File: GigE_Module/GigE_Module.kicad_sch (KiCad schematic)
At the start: 4 parts, among them J1 Conn_01x10_Socket, J3 Conn_01x02_Pin, J4 Conn_01x08_Socket, U4 ENC28J60x-SS

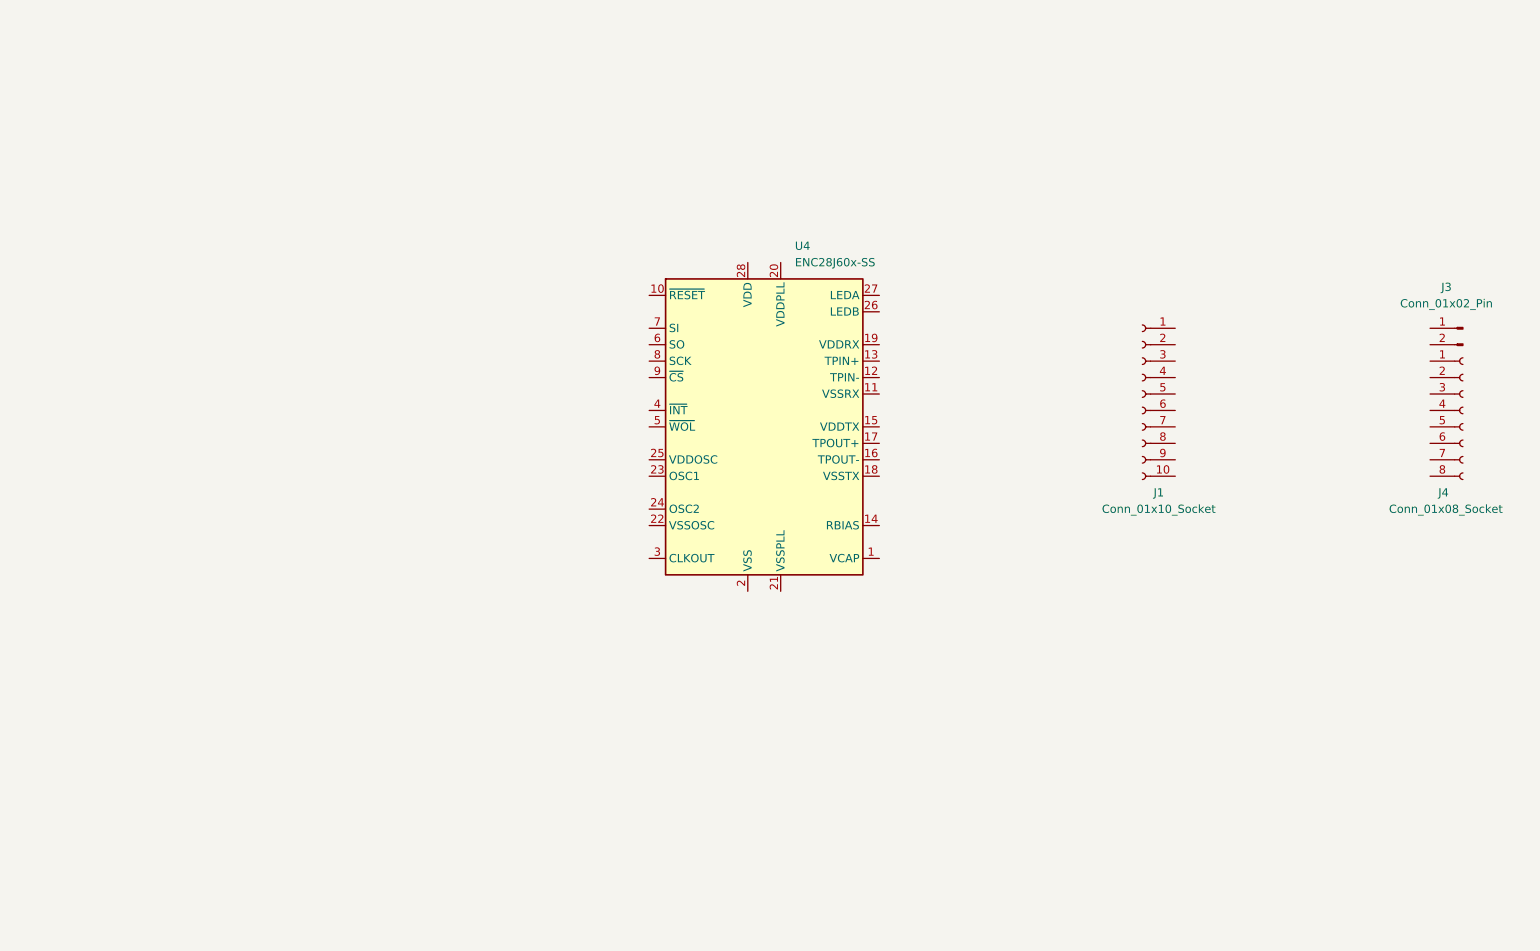
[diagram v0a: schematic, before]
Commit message: Adding GigE PCB design
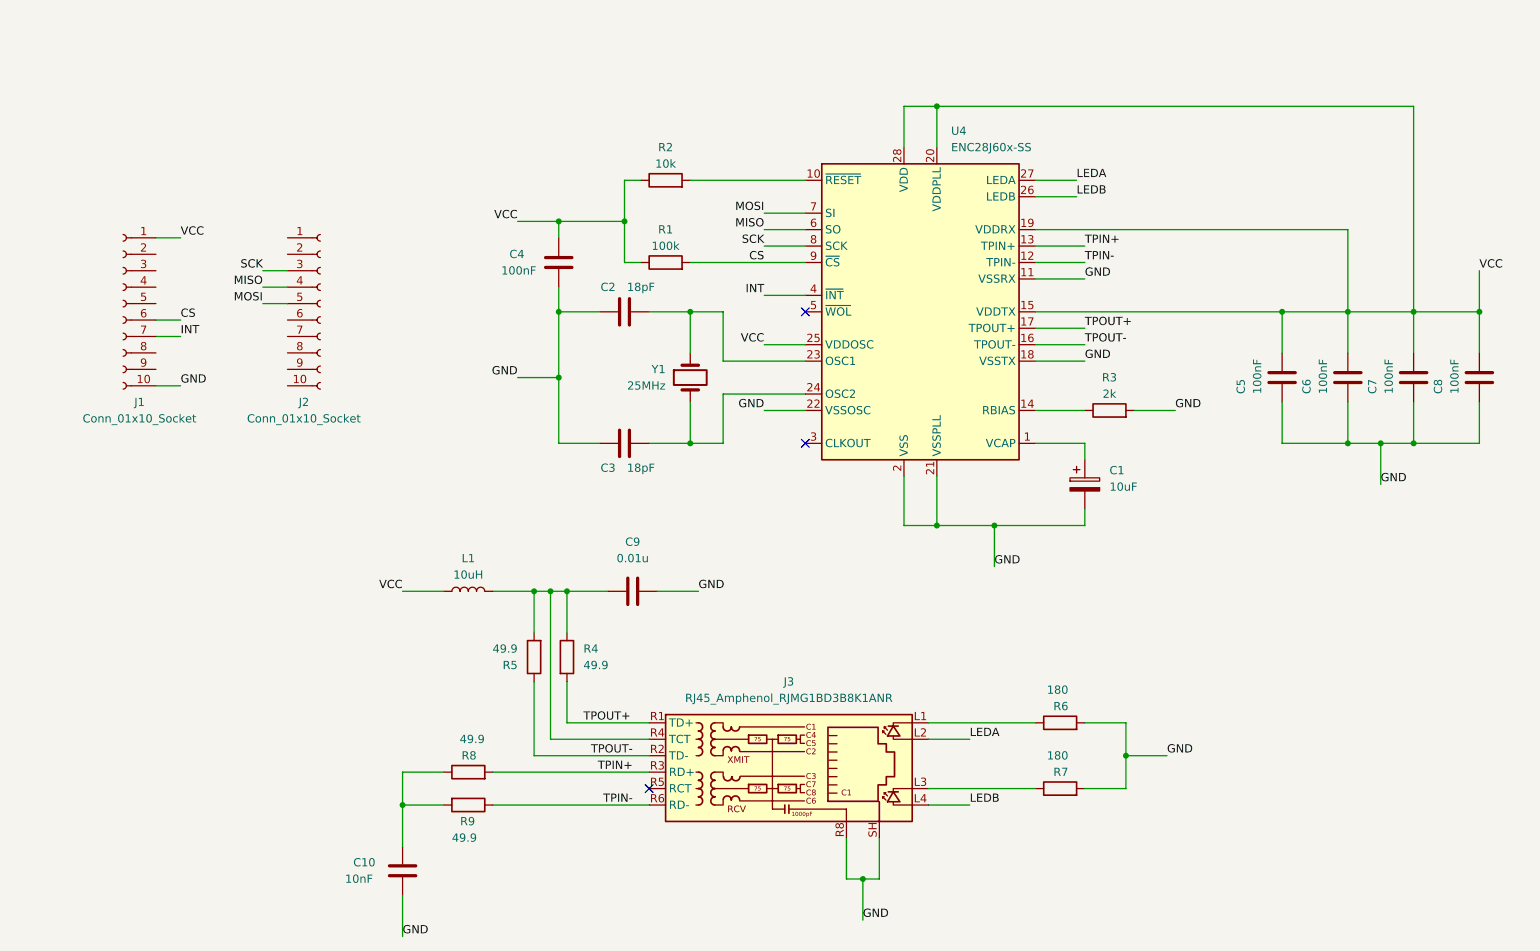
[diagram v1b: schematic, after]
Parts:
- removed J3: Conn_01x02_Pin, Connector_PinHeader_2.00mm:PinHeader_1x02_P2.00mm_Vertical, symbol Connector:Conn_01x02_Pin
- removed J4: Conn_01x08_Socket, Connector_PinSocket_2.00mm:PinSocket_1x08_P2.00mm_Vertical, symbol Connector:Conn_01x08_Socket
- added C1: 10uF, symbol Device:C_Polarized
- added C10: 10nF, symbol Device:C
- added C2, C3: 18pF, symbol Device:C
- added C4, C5, C6, C7, C8: 100nF, symbol Device:C
- added C9: 0.01u, symbol Device:C
- added J2: Conn_01x10_Socket, Connector_PinSocket_2.00mm:PinSocket_1x10_P2.00mm_Vertical, symbol Connector:Conn_01x10_Socket
- added J3: RJ45_Amphenol_RJMG1BD3B8K1ANR, Connector_RJ:RJ45_Amphenol_RJMG1BD3B8K1ANR, symbol Connector:RJ45_Amphenol_RJMG1BD3B8K1ANR
- added L1: 10uH, symbol Device:L
- added R1: 100k, symbol Device:R
- added R2: 10k, symbol Device:R
- added R3: 2k, symbol Device:R
- added R4, R5, R8, R9: 49.9, symbol Device:R
- added R6, R7: 180, symbol Device:R
- added Y1: 25MHz, symbol Device:Crystal
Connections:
- net VCC: now reaches J1.1 (Pin_1)
- net VCC: now also U4.15 (VDDTX), U4.19 (VDDRX), U4.20 (VDDPLL), U4.25 (VDDOSC), U4.28 (VDD), C4.1, C5.1, C6.1, C7.1, C8.1, L1.1, R1.1, R2.1
- net GND: now reaches J1.10 (Pin_10)
- net GND: now also U4.11 (VSSRX), U4.18 (VSSTX), U4.2 (VSS), U4.21 (VSSPLL), U4.22 (VSSOSC), C1.2, C10.2, C2.1, C3.1, C4.2, C5.2, C6.2, C7.2, C8.2, C9.2, J3.R8, J3.SH, R3.2, R6.2, R7.2
- net CS: now reaches J1.6 (Pin_6)
- net CS: now also U4.9 (~{CS}), R1.2
- net INT: now reaches J1.7 (Pin_7)
- net INT: now also U4.4 (~{INT})
- net at U4.1 (VCAP): now also C1.1
- net at U4.10 (~{RESET}): now also R2.2
- net TPIN-: now reaches U4.12 (TPIN-)
- net TPIN-: now also J3.R6 (RD-), R9.1
- net TPIN+: now reaches U4.13 (TPIN+)
- net TPIN+: now also J3.R3 (RD+), R8.2
- net at U4.14 (RBIAS): now also R3.1
- net TPOUT-: now reaches U4.16 (TPOUT-)
- net TPOUT-: now also J3.R2 (TD-), R5.1
- net TPOUT+: now reaches U4.17 (TPOUT+)
- net TPOUT+: now also J3.R1 (TD+), R4.2
- net at U4.23 (OSC1): now also C2.2, Y1.1
- net at U4.24 (OSC2): now also C3.2, Y1.2
- net LEDB: now reaches U4.26 (LEDB)
- net LEDB: now also J3.L4
- net LEDA: now reaches U4.27 (LEDA)
- net LEDA: now also J3.L2
- net MISO: now reaches U4.6 (SO)
- net MISO: now also J2.4 (Pin_4)
- net MOSI: now reaches U4.7 (SI)
- net MOSI: now also J2.5 (Pin_5)
- net SCK: now reaches U4.8 (SCK)
- net SCK: now also J2.3 (Pin_3)
- new net: C9.1, J3.R4 (TCT), L1.2, R4.1, R5.2
- new net: C10.1, R8.1, R9.2
- new net: J3.L1, R6.1
- new net: J3.L3, R7.1
- no-connect marks 0 -> 3
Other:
- moved on the sheet: J1, U4

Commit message: Adding first version of GigE PCB design
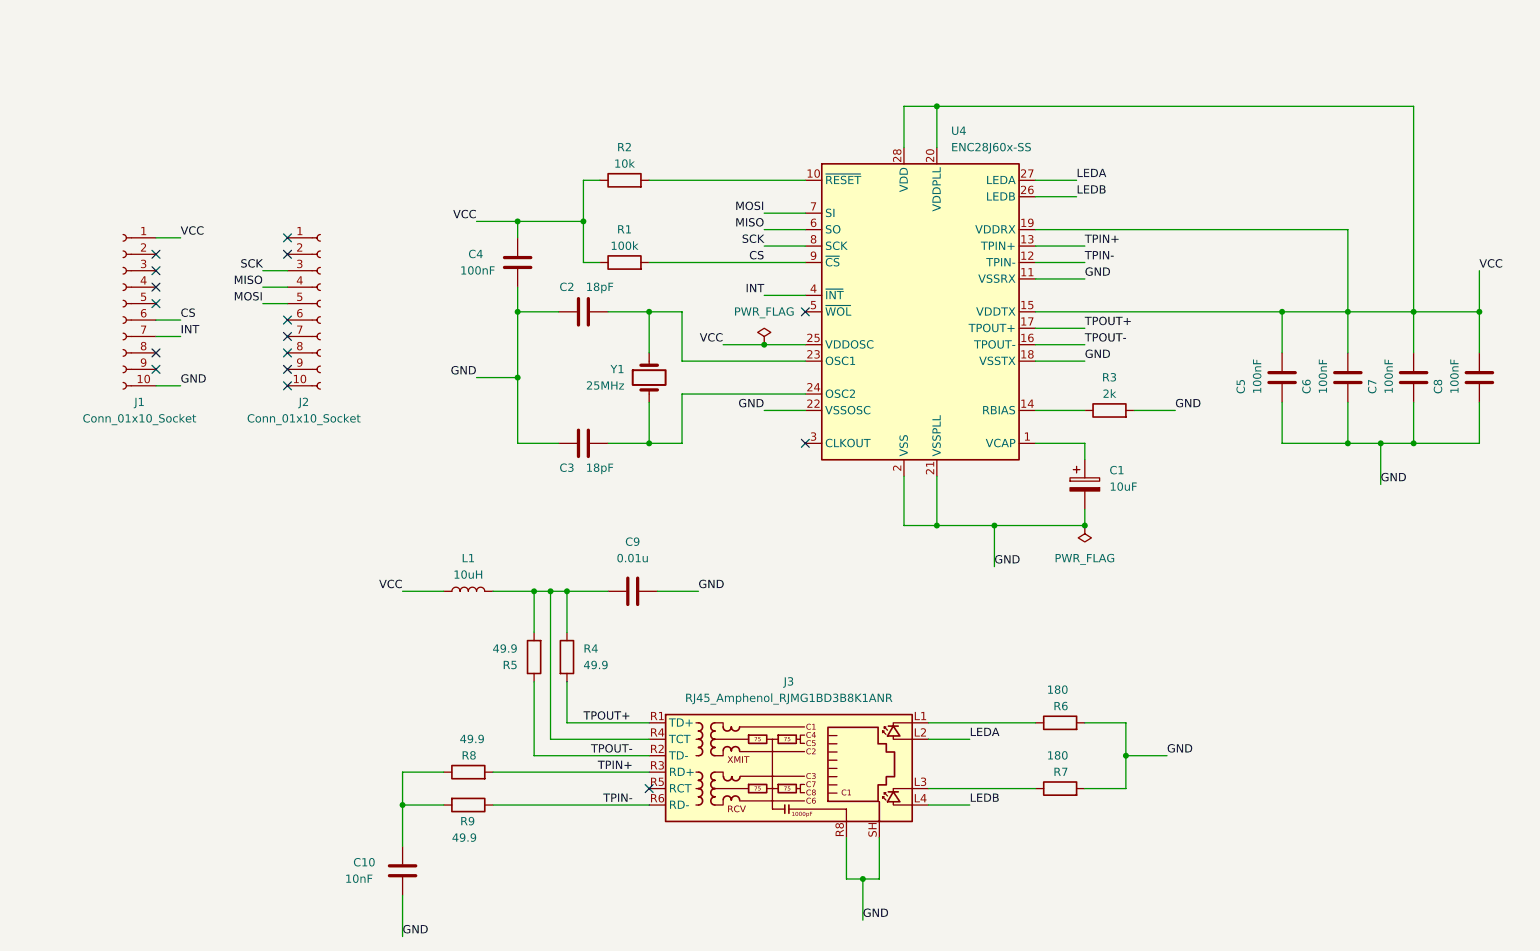
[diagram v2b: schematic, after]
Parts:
- C1, C10, C2, C3, C4, C5, C6, C7, C8, C9: footprint (none) -> Capacitor_Tantalum_SMD:CP_EIA-1608-08_AVX-J
- J3: footprint Connector_RJ:RJ45_Amphenol_RJMG1BD3B8K1ANR -> Connector_RJ:RJ45_Amphenol_RJHSE538X
- L1: footprint (none) -> Inductor_SMD:L_0603_1608Metric
- R1, R2, R3, R4, R5, R6, R7, R8, R9: footprint (none) -> Resistor_SMD:R_0603_1608Metric
- Y1: footprint (none) -> Crystal:Crystal_SMD_MicroCrystal_CC4V-T1A-2Pin_5.0x1.9mm
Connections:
- no-connect marks 3 -> 16
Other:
- moved on the sheet: C2, C3, C4, R1, R2, Y1

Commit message: Finishing GigE PCB design
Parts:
- removed J3: RJ45_Amphenol_RJMG1BD3B8K1ANR, Connector_RJ:RJ45_Amphenol_RJHSE538X, symbol Connector:RJ45_Amphenol_RJMG1BD3B8K1ANR
- added J3: RJ45_LED, Connector_RJ:RJ45_Amphenol_RJHSE538X, symbol Connector:RJ45_LED
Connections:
- net LEDA: now also J3.12
- net LEDB: now also J3.10
- net TPIN+: now also J3.3
- net TPIN-: now also J3.6
- net TPOUT+: now also J3.1
- net TPOUT-: now also J3.2
- net at C9.1, L1.2, R4.1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: now also J3.4
- net at R6.1: now also J3.11
- net at R7.1: now also J3.9
- no-connect marks 16 -> 18
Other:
- moved on the sheet: C1, C2, C3, C4, C5, C6, C7, C8, J1, J2, R1, R2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

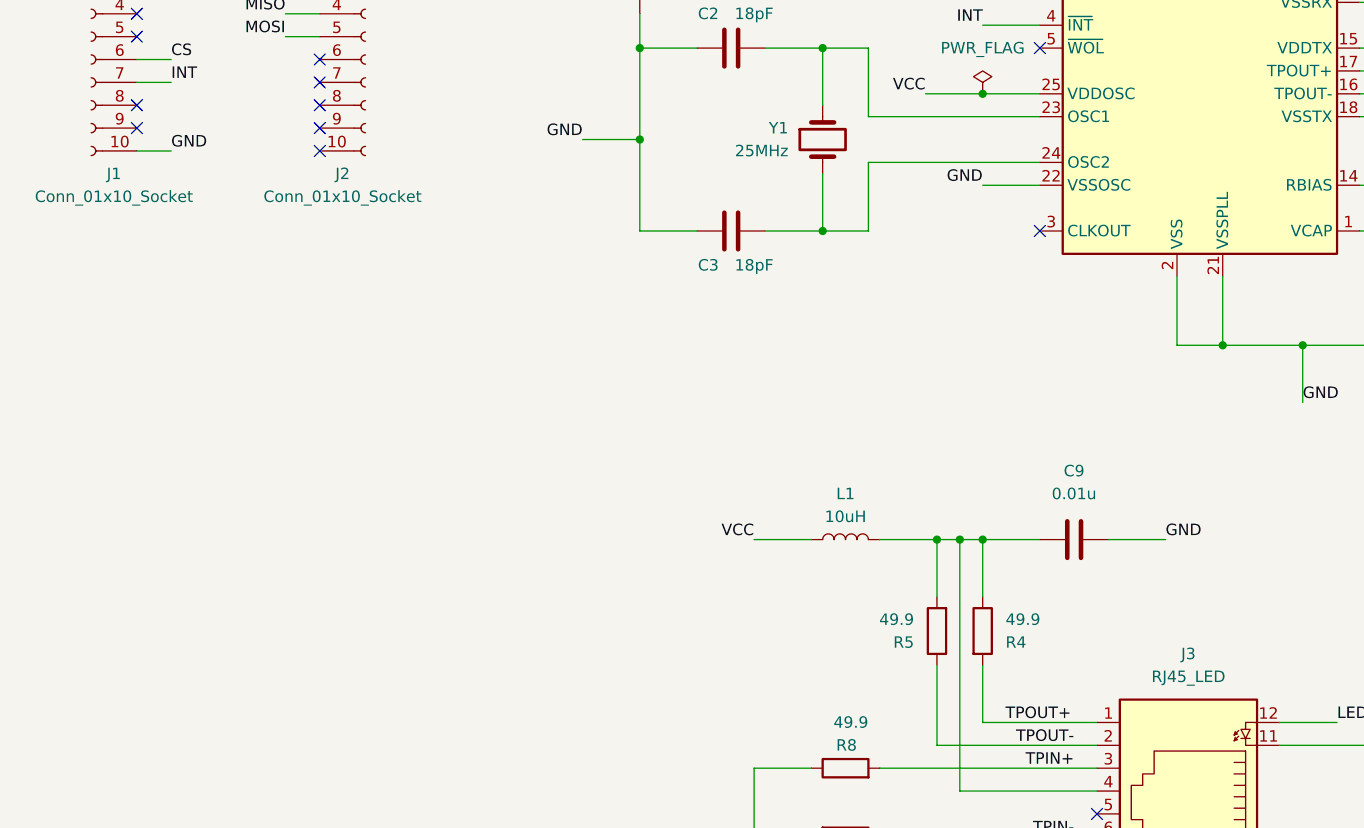
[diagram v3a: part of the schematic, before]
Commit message: Adding FPV 4-pin interface module
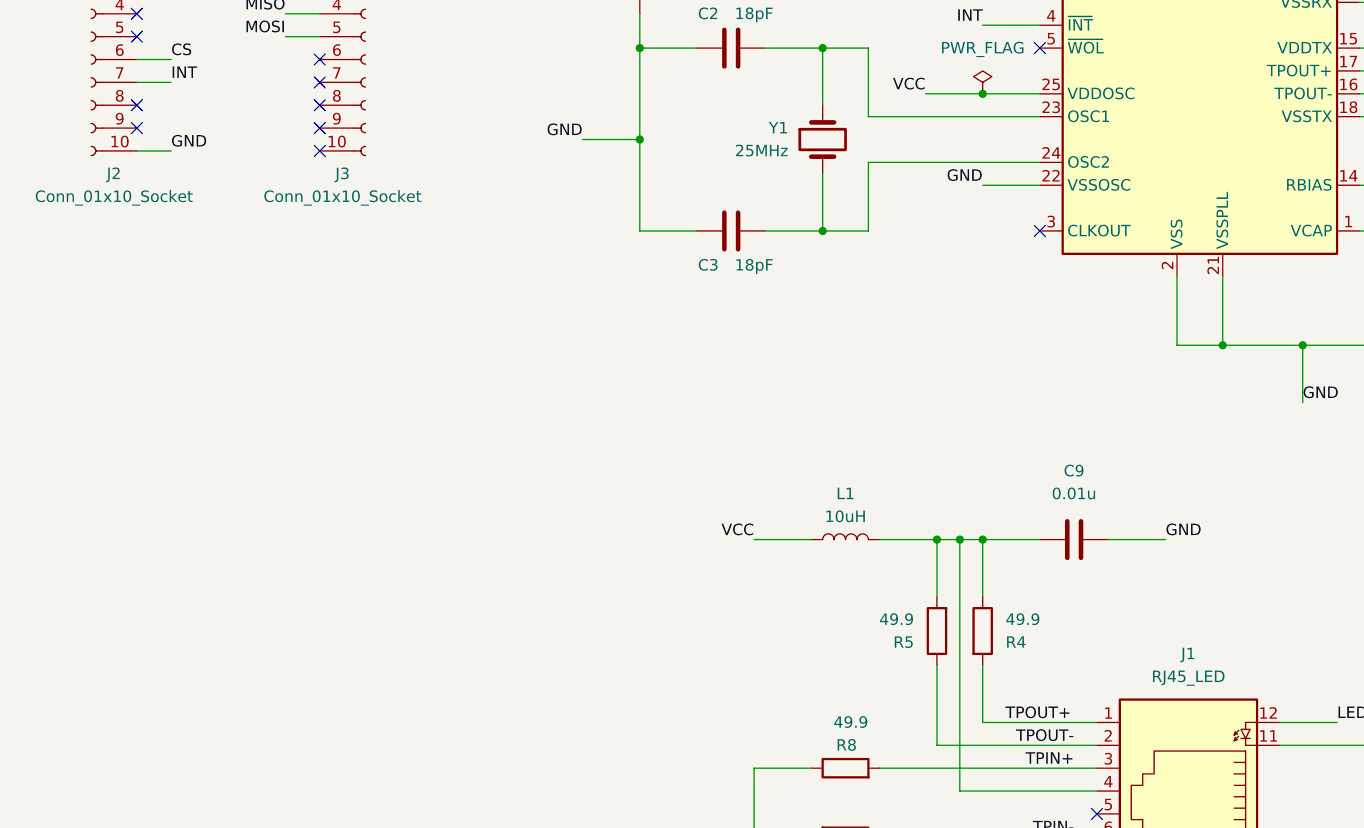
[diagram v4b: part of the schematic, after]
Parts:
- renumbered J3 to J1, J1 to J2, J2 to J3
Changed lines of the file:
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@@
   (symbol (lib_id "Connector:Conn_01x10_Socket") (at 33.02 59.69 0) (mirror y) (unit 1)
     (in_bom yes) (on_board yes) (dnp no)
-    (property "Reference" "J1" (at 35.56 74.93 0)
+    (property "Reference" "J2" (at 35.56 74.93 0)
       (effects (font (size 1.27 1.27)))
     )
@@
       (project "GigE_Module"
         (path "/670fdc0c-f766-4a3d-acb5-c6529564e189"
-          (reference "J1") (unit 1)
+          (reference "J2") (unit 1)
         )
       )
@@
   (symbol (lib_id "Connector:Conn_01x10_Socket") (at 63.5 59.69 0) (unit 1)
     (in_bom yes) (on_board yes) (dnp no)
-    (property "Reference" "J2" (at 60.96 74.93 0)
+    (property "Reference" "J3" (at 60.96 74.93 0)
       (effects (font (size 1.27 1.27)))
     )
@@
       (project "GigE_Module"
         (path "/670fdc0c-f766-4a3d-acb5-c6529564e189"
-          (reference "J2") (unit 1)
+          (reference "J3") (unit 1)
         )
       )
@@
   (symbol (lib_id "Connector:RJ45_LED") (at 154.94 143.51 180) (unit 1)
     (in_bom yes) (on_board yes) (dnp no) (fields_autoplaced)
-    (property "Reference" "J3" (at 154.94 128.27 0)
+    (property "Reference" "J1" (at 154.94 128.27 0)
       (effects (font (size 1.27 1.27)))
     )
@@
       (project "GigE_Module"
         (path "/670fdc0c-f766-4a3d-acb5-c6529564e189"
-          (reference "J3") (unit 1)
-        )
-      )
+          (reference "J1") (unit 1)
+        )
+      )
